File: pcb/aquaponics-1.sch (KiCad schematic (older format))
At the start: 19 parts, among them J1 5V Power Source, J2 Screw_Terminal_01x02, J3 Water Level Sensor, J4 Rain Sensor, J5 Conn_01x02_Female, M1 Growbed Pump, M2 Overflow Pump, M3 Fish Feeder, Q1 TIP120, Q2 TIP120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

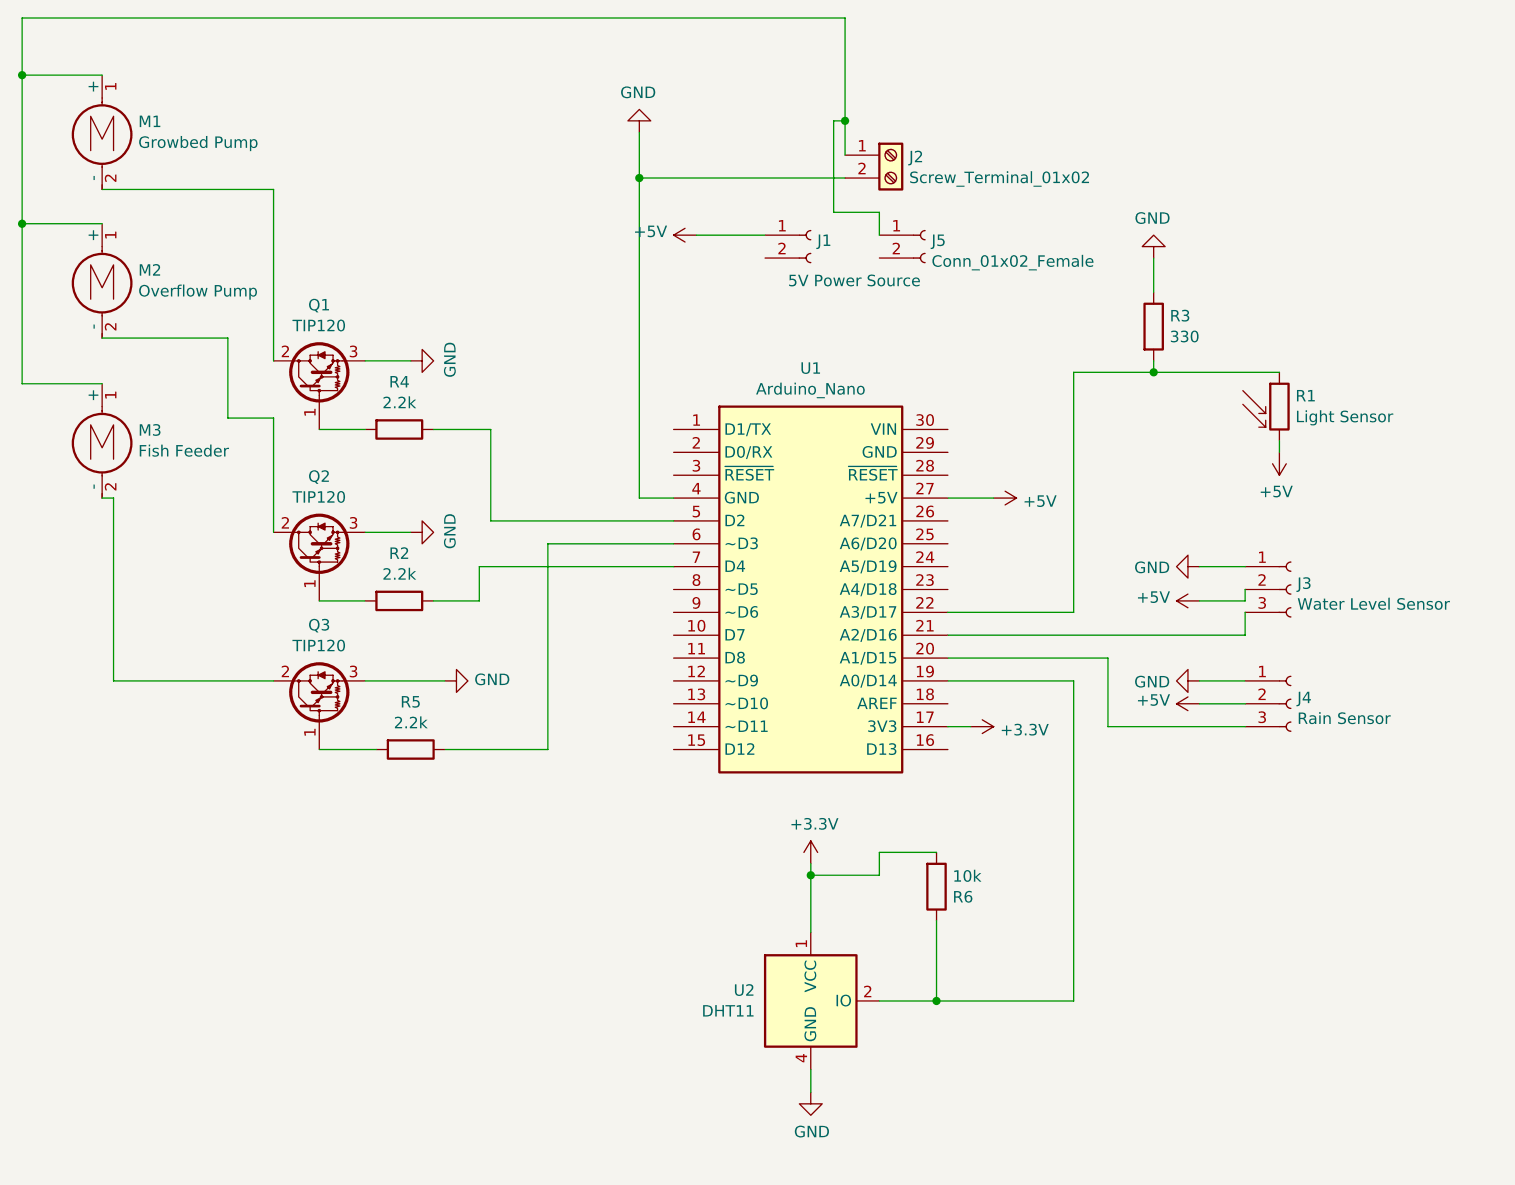
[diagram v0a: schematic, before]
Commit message: Temp sensor to use 5V power
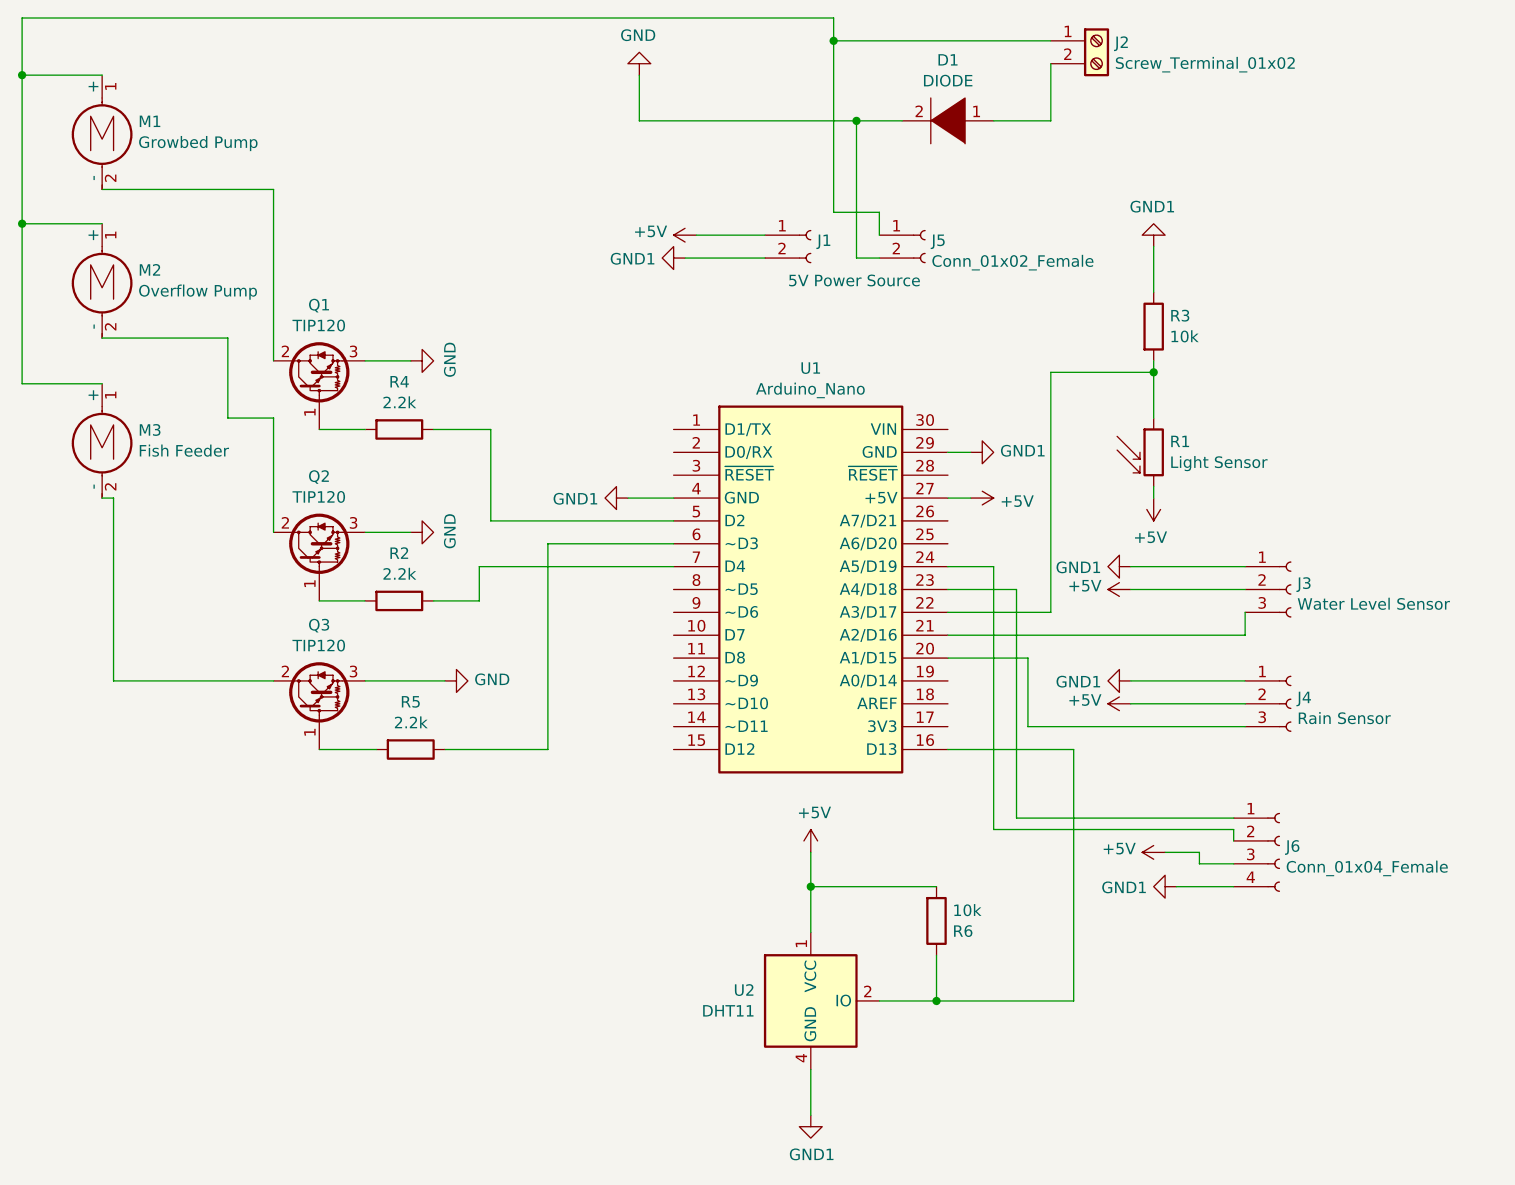
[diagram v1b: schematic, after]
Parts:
- added D1: DIODE, Diode_THT:D_DO-15_P2.54mm_Vertical_AnodeUp, symbol pspice:DIODE
- added J6: Conn_01x04_Female, Connector_PinHeader_2.54mm:PinHeader_1x04_P2.54mm_Vertical, symbol Connector:Conn_01x04_Female
- J1, J5: footprint Connector_TE-Connectivity:TE_826576-2_1x02_P3.96mm_Vertical -> aquaponics-1:VP-TE_826576-2_1x02_P3.96mm_Vertical
- R3: value 330 -> 10k
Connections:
- net +5V: now also R6.2, U2.1 (VCC), J6.3 (Pin_3)
- net GND: now also J5.2 (Pin_2), D1.2 (A); no longer J2.2 (Pin_2), J3.1 (Pin_1), J4.1 (Pin_1), R3.1, U1.4 (GND), U2.4 (GND)
- net at U1.16 (D13): now also R6.1, U2.2 (IO)
- net at U1.23 (A4/D18): now also J6.1 (Pin_1)
- net at U1.24 (A5/D19): now also J6.2 (Pin_2)
- net GND1: now reaches U1.29 (GND)
- net GND1: now also J1.2 (Pin_2), J3.1 (Pin_1), J4.1 (Pin_1), R3.1, U1.4 (GND), U2.4 (GND), J6.4 (Pin_4)
- removed net +3V3: R6.2, U1.17 (3V3), U2.1 (VCC)
- new net: D1.1 (K), J2.2 (Pin_2)
- now unconnected: U1.19 (A0/D14)
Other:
- moved on the sheet: J2, R1, R6
